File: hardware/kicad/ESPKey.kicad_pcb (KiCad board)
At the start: 2 copper layers, 16 x 20 mm, 32 parts, among them P1 Power, P2 Wiegand, Q1 2N7002, Q2 2N7002, Q3 2N7002, U1 RT6212A/B, U2 ESP-12

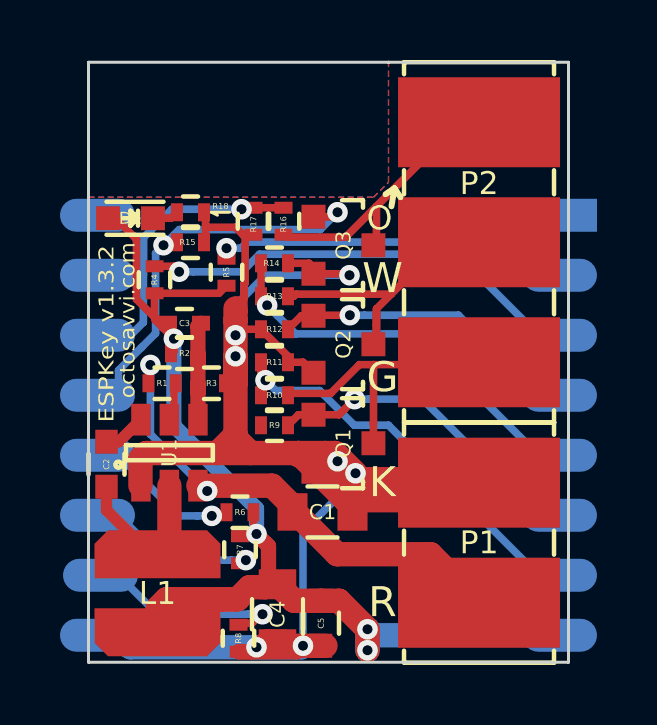
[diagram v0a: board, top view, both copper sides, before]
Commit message: Remove url from front silkscreen
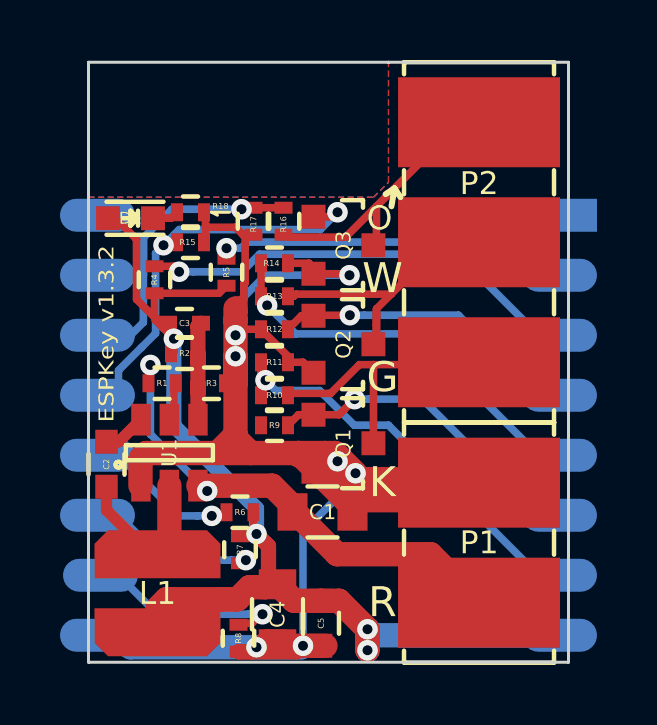
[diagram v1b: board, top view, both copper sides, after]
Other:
- board text removed: "octosavvi.com"
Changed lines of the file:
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@@
-		)
-	)
-	(gr_text "octosavvi.com"
-		(at 105.3 108.6 90)
-		(layer "F.SilkS")
-		(effects
-			(font
-				(size 0.5 0.525)
-				(thickness 0.08)
-			)
 		)
 	)
